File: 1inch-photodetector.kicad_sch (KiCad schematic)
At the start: 23 parts, among them J1 Conn_01x03, J2 Conn_Coaxial, U1 ADA4898-2, U2 LT3032IDE-12

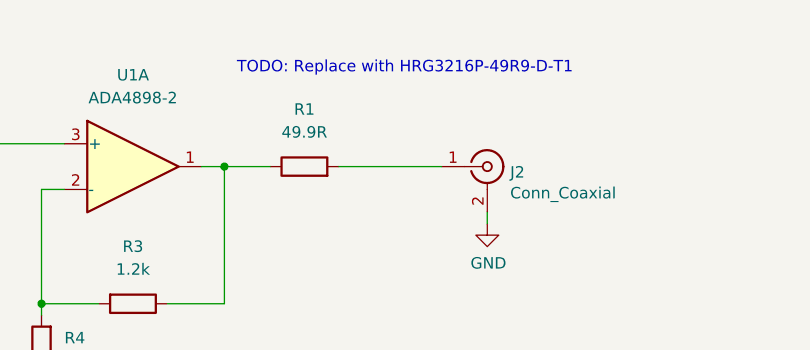
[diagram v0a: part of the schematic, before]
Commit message: Cleanup/remove old refs (#13)
* Removed TODOs that where done

- Fixed R1 MFN

* Added gerber_files folder to gitignore
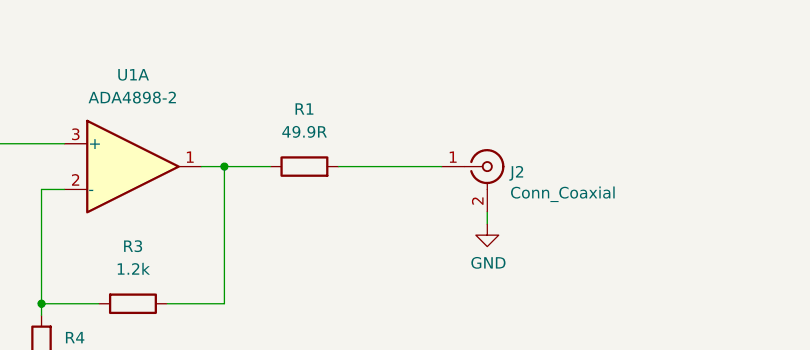
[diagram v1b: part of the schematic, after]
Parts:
- R1: MFN Yageo -> Susumu
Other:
- note removed: "TODO: Replace with HRG3216P-49R9-D-T1"
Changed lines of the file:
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@@
 		(comment 4 "All capacitors are X7R/X8L ceramic unless specified.")
-	)
-	(text "TODO: Replace with HRG3216P-49R9-D-T1"
-		(exclude_from_sim no)
-		(at 164.846 48.768 0)
-		(effects
-			(font
-				(size 1.27 1.27)
-			)
-		)
 	)
 	(junction
@@
 			)
 		)
-		(property "Description" "Susumu"
+		(property "Description" "Resistor"
 			(at 153.67 59.69 0)
 			(effects
@@
 			)
 		)
-		(property "MFN" "Yageo"
+		(property "MFN" "Susumu"
 			(at 153.67 59.69 0)
 			(effects

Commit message: Renamed custom footprint lib
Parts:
- J2: footprint custom_footprints_project:SMP_TE_CONSMP001-SMD-G-T_Vertical -> Custom_footprints_project:SMP_TE_CONSMP001-SMD-G-T_Vertical
- SYM1: footprint custom_footprints_project:QED-logo_small -> Custom_footprints_project:QED-logo_small
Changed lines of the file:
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@@
 			)
 		)
-		(property "Footprint" "custom_footprints_project:SMP_TE_CONSMP001-SMD-G-T_Vertical"
+		(property "Footprint" "Custom_footprints_project:SMP_TE_CONSMP001-SMD-G-T_Vertical"
 			(at 173.99 59.69 0)
 			(effects
@@
 			)
 		)
-		(property "Footprint" "custom_footprints_project:QED-logo_small"
+		(property "Footprint" "Custom_footprints_project:QED-logo_small"
 			(at 255.27 171.45 0)
 			(effects
